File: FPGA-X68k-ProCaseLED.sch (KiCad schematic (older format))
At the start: 109 parts, among them J1 Conn_01x05_Male, J2 Conn_01x04_Male, U1 TLC59116IPWR, U10 TPR-105, U11 TPR-105, U12 TPR-105, U13 TPR-105, U14 TPR-105, U15 TPR-105, U16 TPR-105, U17 TPR-105, U18 TPR-105, U2 MCP23017_SP, U3 TPR-105, U4 TPR-105, U5 TPR-105, U6 TPR-105, U7 TPR-105, U8 TPR-105, U9 TPR-105

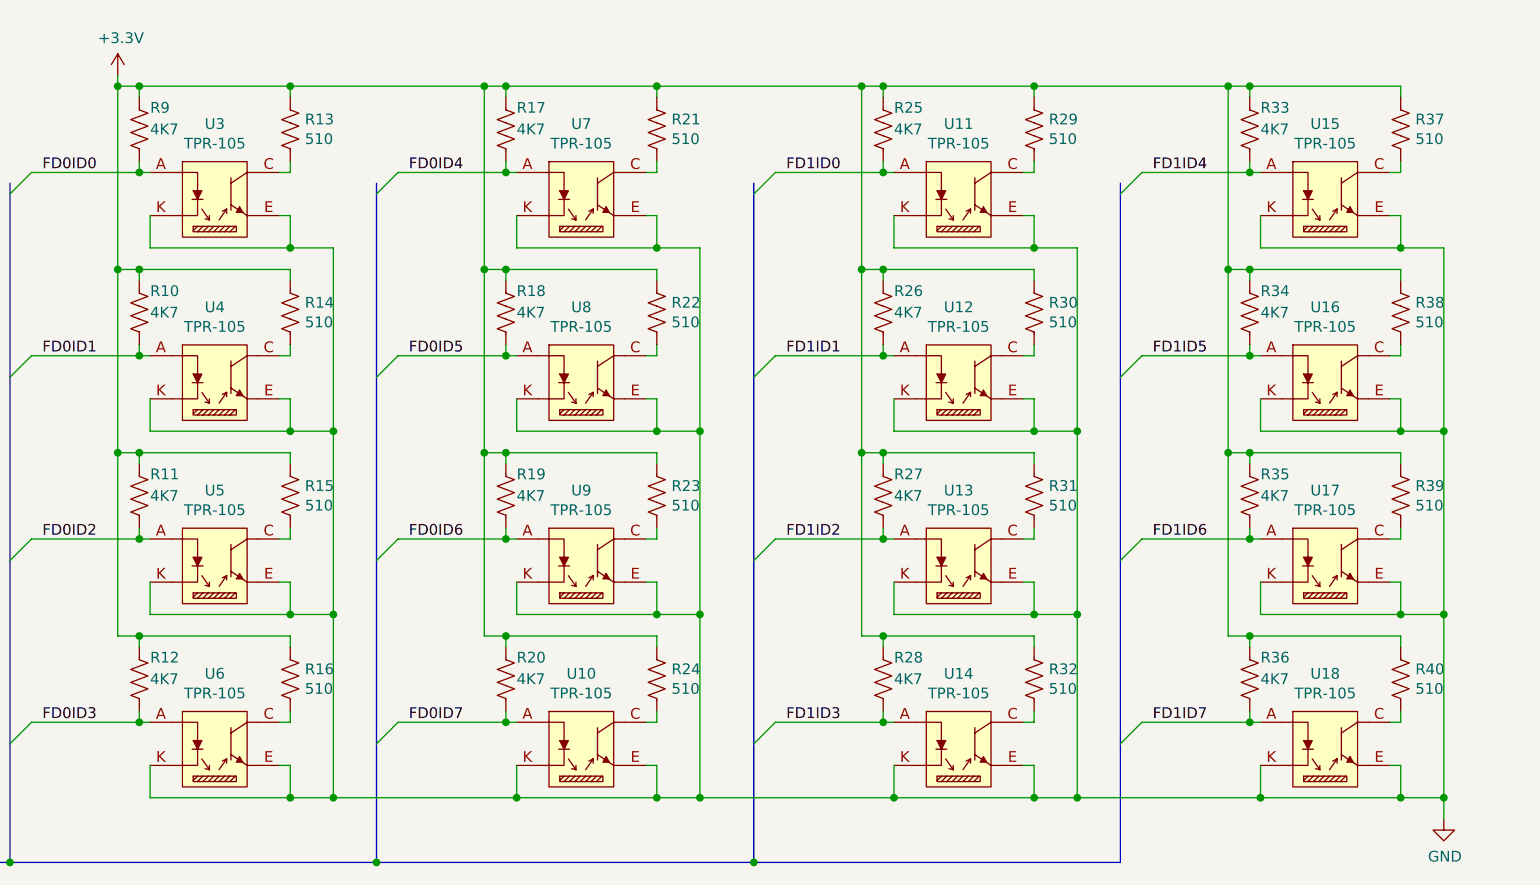
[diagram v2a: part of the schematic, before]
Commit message: Fix the direction of TPR-105.
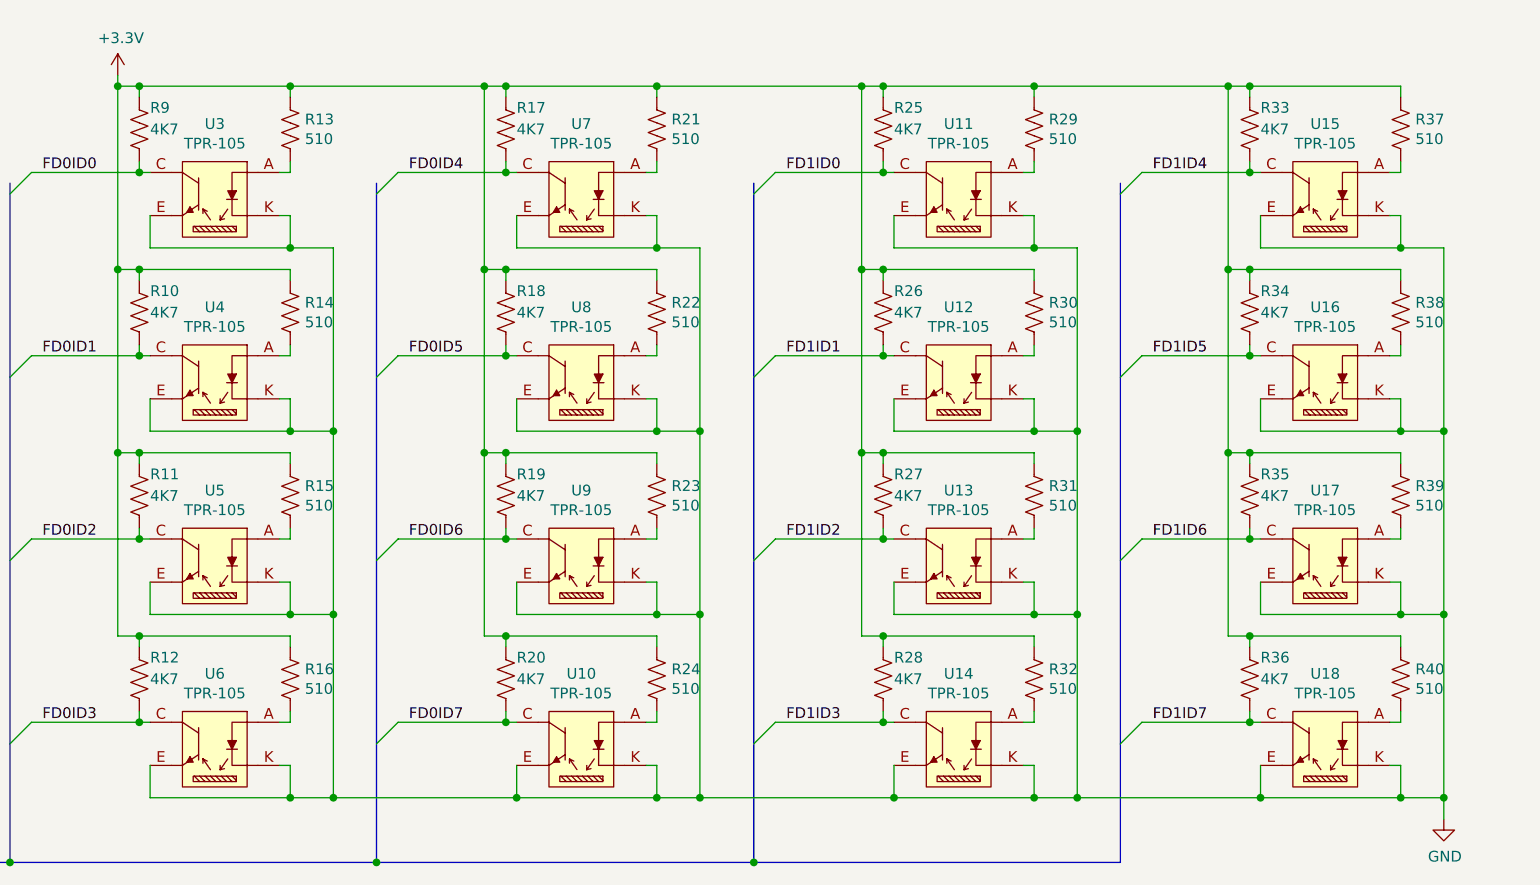
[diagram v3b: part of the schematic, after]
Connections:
- net FD0ID0: now also U3.C; no longer U3.A
- net FD0ID1: now also U4.C; no longer U4.A
- net FD0ID2: now also U5.C; no longer U5.A
- net FD0ID3: now also U6.C; no longer U6.A
- net FD0ID4: now also U7.C; no longer U7.A
- net FD0ID5: now also U8.C; no longer U8.A
- net FD0ID6: now also U9.C; no longer U9.A
- net FD0ID7: now also U10.C; no longer U10.A
- net FD1ID0: now also U11.C; no longer U11.A
- net FD1ID1: now also U12.C; no longer U12.A
- net FD1ID2: now also U13.C; no longer U13.A
- net FD1ID3: now also U14.C; no longer U14.A
- net FD1ID4: now also U15.C; no longer U15.A
- net FD1ID5: now also U16.C; no longer U16.A
- net FD1ID6: now also U17.C; no longer U17.A
- net FD1ID7: now also U18.C; no longer U18.A
- net at R13.1: now also U3.A; no longer U3.C
- net at R14.1: now also U4.A; no longer U4.C
- net at R15.1: now also U5.A; no longer U5.C
- net at R16.1: now also U6.A; no longer U6.C
- net at R21.1: now also U7.A; no longer U7.C
- net at R22.1: now also U8.A; no longer U8.C
- net at R23.1: now also U9.A; no longer U9.C
- net at R24.1: now also U10.A; no longer U10.C
- net at R29.1: now also U11.A; no longer U11.C
- net at R30.1: now also U12.A; no longer U12.C
- net at R31.1: now also U13.A; no longer U13.C
- net at R32.1: now also U14.A; no longer U14.C
- net at R37.1: now also U15.A; no longer U15.C
- net at R38.1: now also U16.A; no longer U16.C
- net at R39.1: now also U17.A; no longer U17.C
- net at R40.1: now also U18.A; no longer U18.C
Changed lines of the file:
@@
 Wire Wire Line
 	7150 8050 7150 8900
-Wire Bus Line
-	3600 10900 3950 10900
-Wire Bus Line
-	3950 10900 5650 10900
-Connection ~ 3950 10900
 $Comp
 L Device:R_US R29
@@
 Wire Wire Line
 	7900 7300 8000 7300
-Wire Wire Line
-	7900 7300 7900 8150
-Wire Wire Line
-	7900 8150 8000 8150
 Connection ~ 7900 7300
 Connection ~ 8000 8150
@@
 Wire Wire Line
 	8000 9850 8000 9900
-Wire Wire Line
-	7900 9000 8000 9000
-Wire Wire Line
-	7900 9000 7900 9850
-Wire Wire Line
-	7900 9850 8000 9850
 Connection ~ 8000 9850
-Wire Wire Line
-	7900 8150 7900 9000
-Connection ~ 7900 8150
-Connection ~ 7900 9000
 Wire Wire Line
 	8700 10600 8900 10600
@@
 Wire Wire Line
 	10600 8050 10600 8900
-Connection ~ 5650 10900
 Wire Wire Line
 	5450 10600 6300 10600
@@
 Connection ~ 10600 10600
 Entry Wire Line
-	9100 7800 9200 7700
-Wire Wire Line
-	9200 7700 9700 7700
-Connection ~ 9700 7700
-Entry Wire Line
-	9100 8650 9200 8550
-Wire Wire Line
-	9200 8550 9700 8550
-Entry Wire Line
-	9100 9500 9200 9400
-Wire Wire Line
-	9200 9400 9700 9400
-Entry Wire Line
-	9100 10350 9200 10250
-Wire Wire Line
-	9200 10250 9700 10250
-Entry Wire Line
-	7400 7800 7500 7700
-Wire Wire Line
-	7500 7700 8000 7700
-Entry Wire Line
-	7400 8650 7500 8550
-Wire Wire Line
-	7500 8550 8000 8550
-Entry Wire Line
-	7400 9500 7500 9400
-Wire Wire Line
-	7500 9400 8000 9400
-Entry Wire Line
-	7400 10350 7500 10250
-Wire Wire Line
-	7500 10250 8000 10250
-Entry Wire Line
-	5650 7800 5750 7700
-Wire Wire Line
-	5750 7700 6250 7700
-Entry Wire Line
-	5650 8650 5750 8550
-Wire Wire Line
-	5750 8550 6250 8550
-Entry Wire Line
-	5650 9500 5750 9400
-Wire Wire Line
-	5750 9400 6250 9400
-Entry Wire Line
-	5650 10350 5750 10250
-Wire Wire Line
-	5750 10250 6250 10250
-Entry Wire Line
-	3950 7800 4050 7700
-Wire Wire Line
-	4050 7700 4550 7700
-Entry Wire Line
-	3950 8650 4050 8550
-Wire Wire Line
-	4050 8550 4550 8550
-Entry Wire Line
-	3950 9500 4050 9400
-Wire Wire Line
-	4050 9400 4550 9400
-Entry Wire Line
-	3950 10350 4050 10250
-Wire Wire Line
-	4050 10250 4550 10250
-Wire Bus Line
-	5650 10900 7400 10900
-Connection ~ 7400 10900
-Wire Bus Line
-	7400 10900 9100 10900
-Entry Wire Line
 	3600 8050 3500 7950
 Entry Wire Line
@@
 Entry Wire Line
 	3600 9650 3500 9550
-Connection ~ 4550 7700
-Connection ~ 4550 8550
-Connection ~ 4550 9400
-Connection ~ 4550 10250
-Connection ~ 6250 7700
-Connection ~ 6250 8550
-Connection ~ 6250 9400
-Connection ~ 6250 10250
-Connection ~ 8000 7700
-Connection ~ 8000 8550
-Connection ~ 8000 9400
-Connection ~ 8000 10250
-Connection ~ 9700 8550
-Connection ~ 9700 9400
-Connection ~ 9700 10250
 Wire Wire Line
 	3050 7950 3500 7950
@@
 Wire Wire Line
 	3050 8650 3500 8650
-$Comp
-L local:TPR-105 U3
-U 1 1 5FD406A0
-P 4900 7550
-F 0 "U3" H 4900 7625 50  0000 C CNN
-F 1 "TPR-105" H 4900 7534 50  0000 C CNN
-F 2 "local:TPR-105" H 4900 7550 50  0001 C CNN
-F 3 "" H 4900 7550 50  0001 C CNN
-	1    4900 7550
-	1    0    0    -1
-$EndComp
 $Comp
 L local:TPR-105 U4
@@
 F 3 "" H 4900 8400 50  0001 C CNN
 	1    4900 8400
-	1    0    0    -1
+	-1   0    0    -1
 $EndComp
 Wire Wire Line
@@
 F 3 "" H 4900 9250 50  0001 C CNN
 	1    4900 9250
-	1    0    0    -1
+	-1   0    0    -1
 $EndComp
 $Comp
@@
 F 3 "" H 4900 10100 50  0001 C CNN
 	1    4900 10100
-	1    0    0    -1
+	-1   0    0    -1
 $EndComp
 $Comp
@@
 F 3 "" H 10050 7550 50  0001 C CNN
 	1    10050 7550
-	1    0    0    -1
+	-1   0    0    -1
 $EndComp
 $Comp
@@
 F 3 "" H 10050 8400 50  0001 C CNN
 	1    10050 8400
-	1    0    0    -1
+	-1   0    0    -1
 $EndComp
 $Comp
@@
 F 3 "" H 10050 9250 50  0001 C CNN
 	1    10050 9250
-	1    0    0    -1
+	-1   0    0    -1
 $EndComp
 $Comp
@@
 F 3 "" H 10050 10100 50  0001 C CNN
 	1    10050 10100
-	1    0    0    -1
+	-1   0    0    -1
 $EndComp
 $Comp
@@
 F 3 "" H 6600 7550 50  0001 C CNN
 	1    6600 7550
-	1    0    0    -1
+	-1   0    0    -1
 $EndComp
 $Comp
@@
 F 3 "" H 6600 8400 50  0001 C CNN
 	1    6600 8400
-	1    0    0    -1
+	-1   0    0    -1
 $EndComp
 $Comp
@@
 F 3 "" H 6600 9250 50  0001 C CNN
 	1    6600 9250
-	1    0    0    -1
+	-1   0    0    -1
 $EndComp
 $Comp
@@
 F 3 "" H 6600 10100 50  0001 C CNN
 	1    6600 10100
-	1    0    0    -1
+	-1   0    0    -1
 $EndComp
 $Comp
@@
 F 3 "" H 8350 7550 50  0001 C CNN
 	1    8350 7550
-	1    0    0    -1
+	-1   0    0    -1
 $EndComp
 $Comp
@@
 F 3 "" H 8350 8400 50  0001 C CNN
 	1    8350 8400
-	1    0    0    -1
+	-1   0    0    -1
 $EndComp
 $Comp
@@
 F 3 "" H 8350 9250 50  0001 C CNN
 	1    8350 9250
-	1    0    0    -1
+	-1   0    0    -1
 $EndComp
 $Comp
@@
 F 3 "" H 8350 10100 50  0001 C CNN
 	1    8350 10100
-	1    0    0    -1
+	-1   0    0    -1
 $EndComp
 Text Label 3100 7950 0    50   ~ 0
@@
 Text Label 3100 9550 0    50   ~ 0
 FD0ID7
-Text Label 4100 7700 0    50   ~ 0
-FD0ID0
-Text Label 4100 8550 0    50   ~ 0
-FD0ID1
-Text Label 4100 9400 0    50   ~ 0
-FD0ID2
-Text Label 4100 10250 0    50   ~ 0
-FD0ID3
-Text Label 5800 7700 0    50   ~ 0
-FD0ID4
-Text Label 5800 8550 0    50   ~ 0
-FD0ID5
-Text Label 5800 9400 0    50   ~ 0
-FD0ID6
-Text Label 5800 10250 0    50   ~ 0
-FD0ID7
-Text Label 7550 7700 0    50   ~ 0
-FD1ID0
-Text Label 7550 8550 0    50   ~ 0
-FD1ID1
-Text Label 7550 9400 0    50   ~ 0
-FD1ID2
-Text Label 7550 10250 0    50   ~ 0
-FD1ID3
-Text Label 9250 7700 0    50   ~ 0
-FD1ID4
-Text Label 9250 8550 0    50   ~ 0
-FD1ID5
-Text Label 9250 9400 0    50   ~ 0
-FD1ID6
-Text Label 9250 10250 0    50   ~ 0
-FD1ID7
 $Comp
 L power:GND #PWR014
@@
 Wire Wire Line
 	2350 7500 2850 7500
+Connection ~ 2350 7500
+Wire Wire Line
+	2350 7500 2350 7650
+Connection ~ 7900 9000
+Connection ~ 7900 8150
+Wire Wire Line
+	7900 8150 7900 9000
+Wire Wire Line
+	7900 9850 8000 9850
+Wire Wire Line
+	7900 9000 7900 9850
+Wire Wire Line
+	7900 9000 8000 9000
+Wire Wire Line
+	7900 8150 8000 8150
+Wire Wire Line
+	7900 7300 7900 8150
+$Comp
+L local:TPR-105 U3
+U 1 1 5FD406A0
+P 4900 7550
+F 0 "U3" H 4900 7625 50  0000 C CNN
+F 1 "TPR-105" H 4900 7534 50  0000 C CNN
+F 2 "local:TPR-105" H 4900 7550 50  0001 C CNN
+F 3 "" H 4900 7550 50  0001 C CNN
+	1    4900 7550
+	-1   0    0    -1
+$EndComp
+Wire Bus Line
+	3600 10900 3950 10900
+Connection ~ 3950 10900
+Connection ~ 4550 10250
+Connection ~ 4550 9400
+Connection ~ 4550 8550
+Connection ~ 4550 7700
+Text Label 4100 10250 0    50   ~ 0
+FD0ID3
+Text Label 4100 9400 0    50   ~ 0
+FD0ID2
+Text Label 4100 8550 0    50   ~ 0
+FD0ID1
+Text Label 4100 7700 0    50   ~ 0
+FD0ID0
+Wire Wire Line
+	4050 10250 4550 10250
+Entry Wire Line
+	3950 10350 4050 10250
+Wire Wire Line
+	4050 9400 4550 9400
+Entry Wire Line
+	3950 9500 4050 9400
+Wire Wire Line
+	4050 8550 4550 8550
+Entry Wire Line
+	3950 8650 4050 8550
+Wire Wire Line
+	4050 7700 4550 7700
+Entry Wire Line
+	3950 7800 4050 7700
+Wire Bus Line
+	3950 10900 5650 10900
+Connection ~ 5650 10900
+Connection ~ 6250 10250
+Connection ~ 6250 9400
+Connection ~ 6250 8550
+Connection ~ 6250 7700
+Text Label 5800 10250 0    50   ~ 0
+FD0ID7
+Text Label 5800 9400 0    50   ~ 0
+FD0ID6
+Text Label 5800 8550 0    50   ~ 0
+FD0ID5
+Text Label 5800 7700 0    50   ~ 0
+FD0ID4
+Wire Wire Line
+	5750 10250 6250 10250
+Entry Wire Line
+	5650 10350 5750 10250
+Wire Wire Line
+	5750 9400 6250 9400
+Entry Wire Line
+	5650 9500 5750 9400
+Wire Wire Line
+	5750 8550 6250 8550
+Entry Wire Line
+	5650 8650 5750 8550
+Wire Wire Line
+	5750 7700 6250 7700
+Entry Wire Line
+	5650 7800 5750 7700
+Wire Bus Line
+	5650 10900 7400 10900
+Connection ~ 7400 10900
+Connection ~ 8000 10250
+Connection ~ 8000 9400
+Connection ~ 8000 8550
+Connection ~ 8000 7700
+Entry Wire Line
+	7400 7800 7500 7700
+Wire Wire Line
+	7500 7700 8000 7700
+Entry Wire Line
+	7400 8650 7500 8550
+Wire Wire Line
+	7500 8550 8000 8550
+Entry Wire Line
+	7400 9500 7500 9400
+Wire Wire Line
+	7500 9400 8000 9400
+Entry Wire Line
+	7400 10350 7500 10250
+Wire Wire Line
+	7500 10250 8000 10250
+Text Label 7550 7700 0    50   ~ 0
+FD1ID0
+Text Label 7550 8550 0    50   ~ 0
+FD1ID1
+Text Label 7550 9400 0    50   ~ 0
+FD1ID2
+Text Label 7550 10250 0    50   ~ 0
+FD1ID3
+Wire Bus Line
+	7400 10900 9100 10900
+Text Label 9250 10250 0    50   ~ 0
+FD1ID7
+Text Label 9250 9400 0    50   ~ 0
+FD1ID6
+Text Label 9250 8550 0    50   ~ 0
+FD1ID5
+Text Label 9250 7700 0    50   ~ 0
+FD1ID4
+Connection ~ 9700 10250
+Wire Wire Line
+	9200 10250 9700 10250
+Entry Wire Line
+	9100 10350 9200 10250
+Connection ~ 9700 9400
+Wire Wire Line
+	9200 9400 9700 9400
+Entry Wire Line
+	9100 9500 9200 9400
+Connection ~ 9700 8550
+Wire Wire Line
+	9200 8550 9700 8550
+Entry Wire Line
+	9100 8650 9200 8550
+Connection ~ 9700 7700
+Wire Wire Line
+	9200 7700 9700 7700
+Entry Wire Line
+	9100 7800 9200 7700
 Wire Bus Line
 	1150 6500 1150 8750
+Wire Bus Line
+	1150 6500 3150 6500
+Wire Bus Line
+	7400 7750 7400 10900
 Wire Bus Line
 	3950 7750 3950 10900
@@
 	5650 7750 5650 10900
 Wire Bus Line
-	7400 7750 7400 10900
-Wire Bus Line
 	9100 7750 9100 10900
-Wire Bus Line
-	1150 6500 3150 6500
 Wire Bus Line
 	3600 7900 3600 10900
@@
 Wire Bus Line
 	5350 2300 5350 6400
-Connection ~ 2350 7500
-Wire Wire Line
-	2350 7500 2350 7650
 $EndSCHEMATC

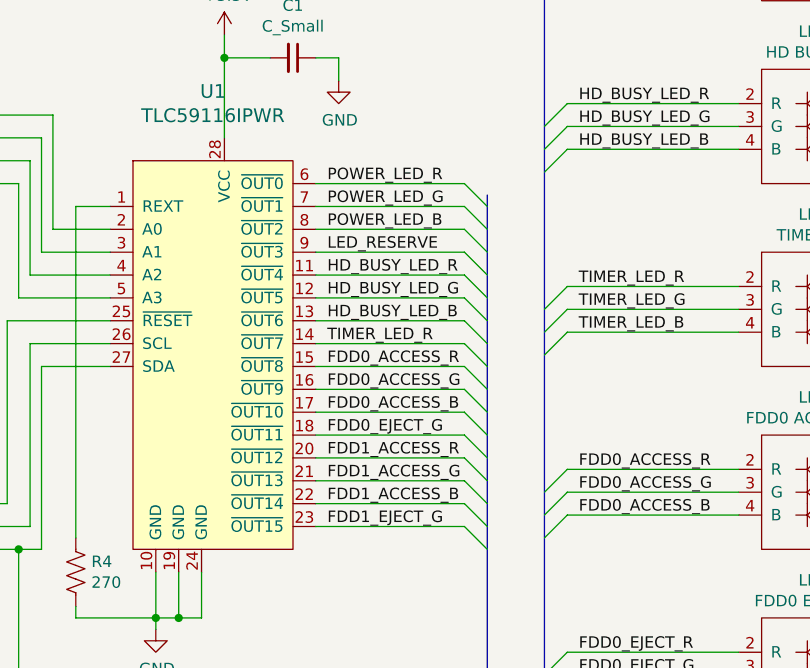
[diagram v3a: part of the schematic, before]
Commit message: Fix LTSN-B32JEGBB-LY's footprint and TIMER LED pattern.
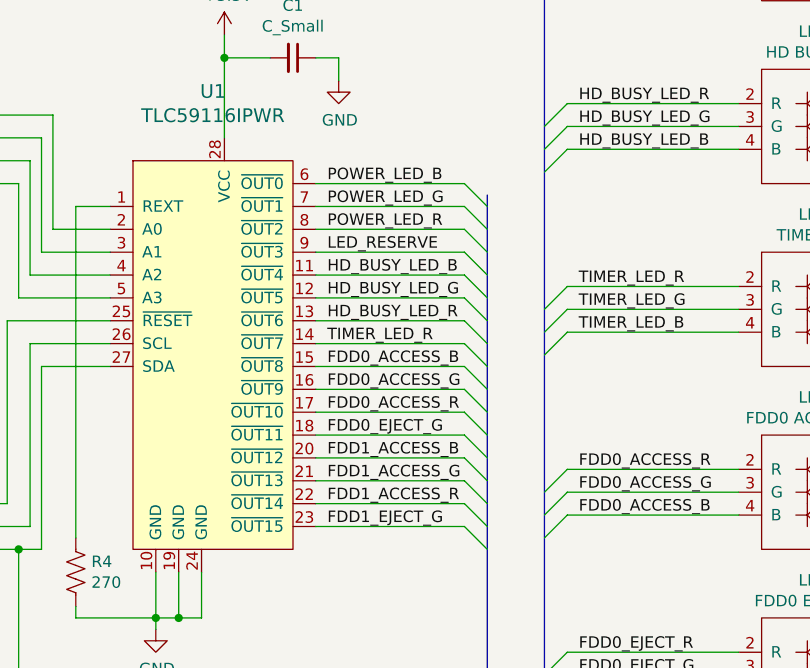
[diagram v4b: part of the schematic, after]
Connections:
- net FDD0_ACCESS_B: now also U1.15 (~OUT8); no longer U1.17 (~OUT10)
- net FDD0_ACCESS_R: now also U1.17 (~OUT10); no longer U1.15 (~OUT8)
- net FDD1_ACCESS_B: now also U1.20 (~OUT12); no longer U1.22 (~OUT14)
- net FDD1_ACCESS_R: now also U1.22 (~OUT14); no longer U1.20 (~OUT12)
- net HD_BUSY_LED_B: now also U1.11 (~OUT4); no longer U1.13 (~OUT6)
- net HD_BUSY_LED_R: now also U1.13 (~OUT6); no longer U1.11 (~OUT4)
- net POWER_LED_B: now also U1.6 (~OUT0); no longer U1.8 (~OUT2)
- net POWER_LED_R: now also U1.8 (~OUT2); no longer U1.6 (~OUT0)
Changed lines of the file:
@@
 Wire Wire Line
 	5700 6100 6450 6100
-Text Label 4650 2250 0    50   ~ 0
-POWER_LED_R
 Text Label 4650 2350 0    50   ~ 0
 POWER_LED_G
 Text Label 4650 2450 0    50   ~ 0
-POWER_LED_B
+POWER_LED_R
 Text Label 4650 2550 0    50   ~ 0
 LED_RESERVE
 Text Label 4650 2650 0    50   ~ 0
-HD_BUSY_LED_R
+HD_BUSY_LED_B
 Text Label 4650 2750 0    50   ~ 0
 HD_BUSY_LED_G
 Text Label 4650 2850 0    50   ~ 0
-HD_BUSY_LED_B
+HD_BUSY_LED_R
 Text Label 4650 2950 0    50   ~ 0
 TIMER_LED_R
 Text Label 4650 3050 0    50   ~ 0
-FDD0_ACCESS_R
+FDD0_ACCESS_B
 Text Label 4650 3150 0    50   ~ 0
 FDD0_ACCESS_G
 Text Label 4650 3250 0    50   ~ 0
-FDD0_ACCESS_B
+FDD0_ACCESS_R
 Text Label 4650 3350 0    50   ~ 0
 FDD0_EJECT_G
 Text Label 4650 3450 0    50   ~ 0
-FDD1_ACCESS_R
+FDD1_ACCESS_B
 Text Label 4650 3550 0    50   ~ 0
 FDD1_ACCESS_G
 Text Label 4650 3650 0    50   ~ 0
-FDD1_ACCESS_B
+FDD1_ACCESS_R
 Text Label 4650 3750 0    50   ~ 0
 FDD1_EJECT_G
-Text Label 5750 1100 0    50   ~ 0
-POWER_LED_R
 Text Label 5750 1200 0    50   ~ 0
 POWER_LED_G
-Text Label 5750 1300 0    50   ~ 0
-POWER_LED_B
-Text Label 5750 1900 0    50   ~ 0
-HD_BUSY_LED_R
 Text Label 5750 2000 0    50   ~ 0
 HD_BUSY_LED_G
-Text Label 5750 2100 0    50   ~ 0
-HD_BUSY_LED_B
 Text Label 5750 2700 0    50   ~ 0
 TIMER_LED_R
@@
 Wire Bus Line
 	5350 2300 5350 6400
+Text Label 5750 2100 0    50   ~ 0
+HD_BUSY_LED_B
+Text Label 5750 1900 0    50   ~ 0
+HD_BUSY_LED_R
+Text Label 5750 1300 0    50   ~ 0
+POWER_LED_B
+Text Label 5750 1100 0    50   ~ 0
+POWER_LED_R
+Text Label 4650 2250 0    50   ~ 0
+POWER_LED_B
 $EndSCHEMATC
